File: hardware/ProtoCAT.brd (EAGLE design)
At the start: 59.7 x 53.3 mm, 47 parts, among them U1 ARDUINO, U3 TB6621FNG

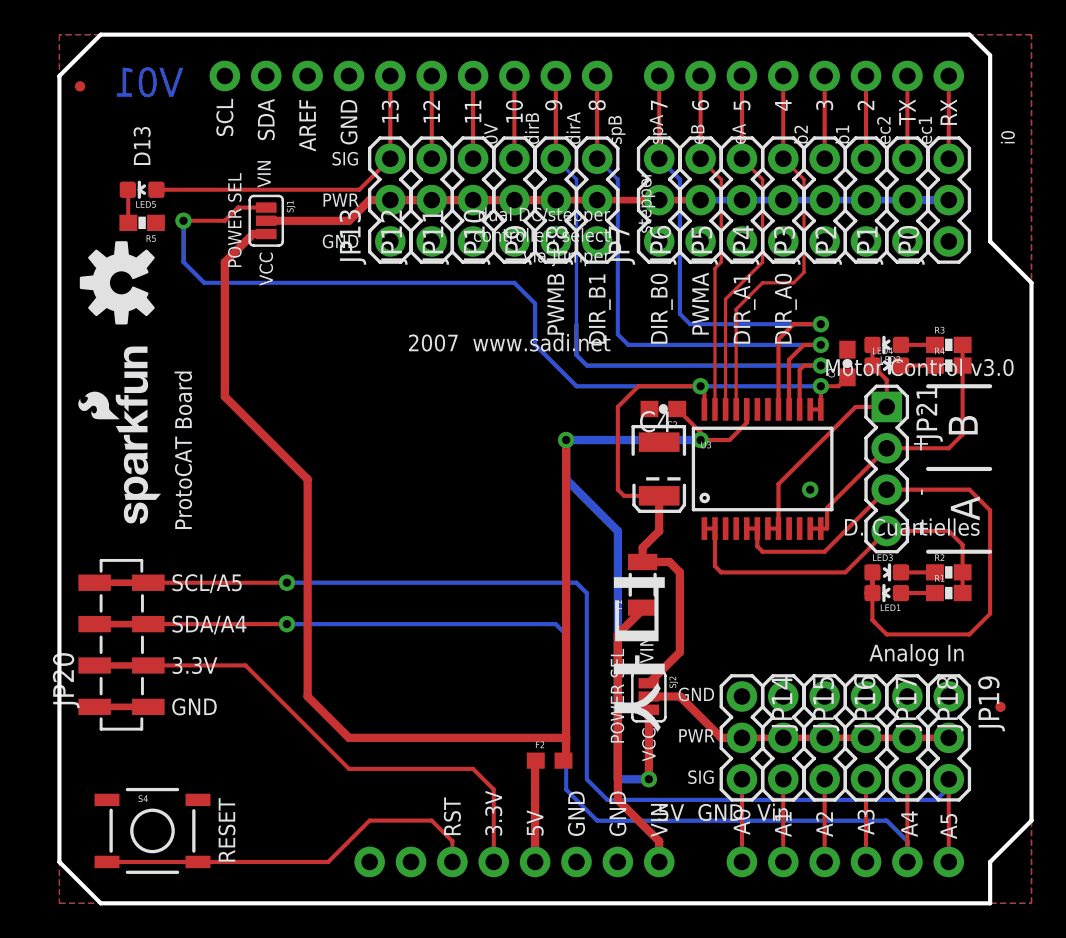
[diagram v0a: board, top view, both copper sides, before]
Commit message: Updates per - engineering review mtg 8/18
added prototyping area
added cut/solder jumpers for A4/A5 SDA/SCL lines for Leo
added ~PWM labels on pins 3, 5, 6, 9, 10, 11
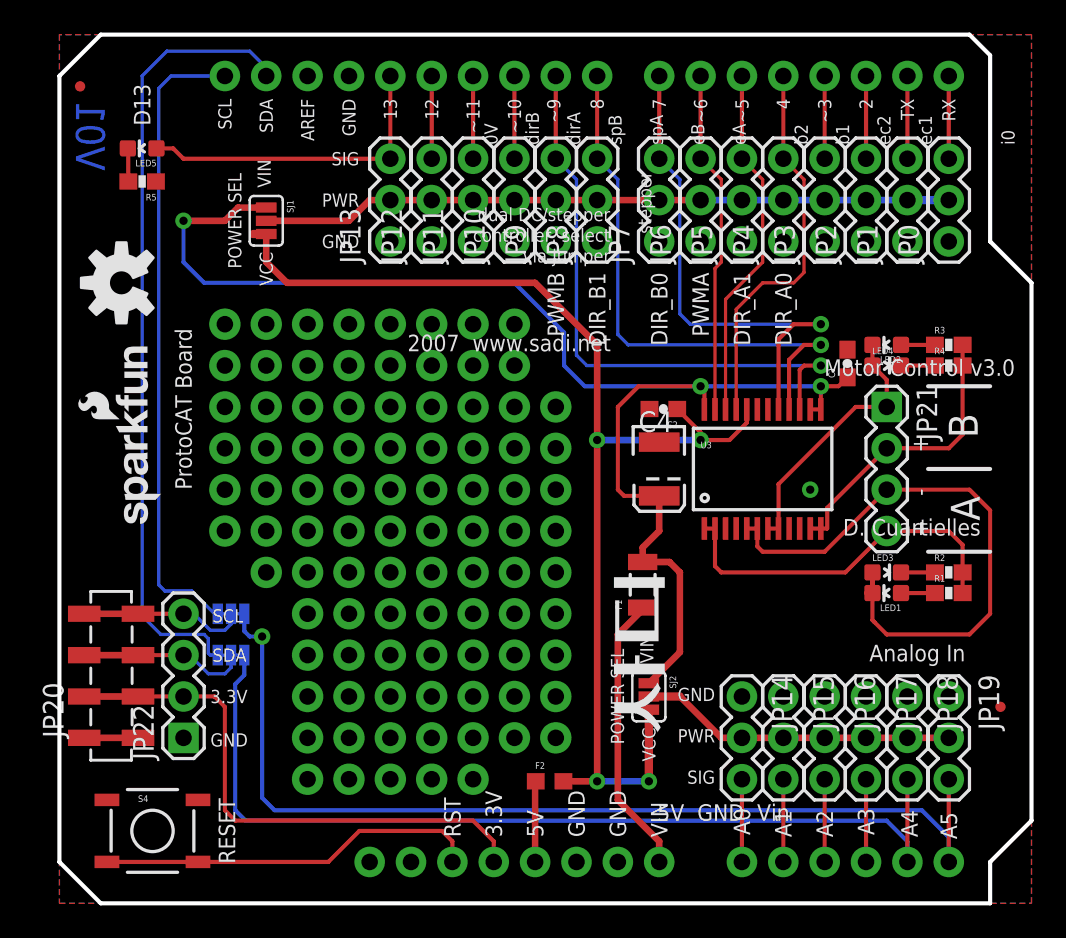
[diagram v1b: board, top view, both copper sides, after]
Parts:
- added JP22: (no value), SparkFun-Connectors:1X04
- added SJ3, SJ4: (no value), SparkFun-Passives:PAD-JUMPER-3-3OF3_NC_BY_TRACE_YES_SILK_FULL_BOX
- JP0: value (none) -> D0
- JP1: value (none) -> D1
- JP10: value (none) -> D10
- JP11: value (none) -> D11
- JP12: value (none) -> D12
- JP13: value (none) -> D13
- JP14: value (none) -> A0
- JP15: value (none) -> A1
- JP16: value (none) -> A2
- JP17: value (none) -> A3
- JP18: value (none) -> A4
- JP19: value (none) -> A5
- JP2: value (none) -> D2
- JP3: value (none) -> D3
- JP4: value (none) -> D4
- JP5: value (none) -> D5
- JP6: value (none) -> D6
- JP7: value (none) -> D7
- JP8: value (none) -> D8
- JP9: value (none) -> D9
- LED5: value (none) -> YELLOW
- LOGO2: value (none) -> SFE_LOGO_NAME_FLAME.1_INCH
- S4: value (none) -> RESET
- moved LED5 2.54 mm to (5.08, 46.4)
- moved R5 2.54 mm to (5.08, 44.3)
- moved JP20 2.01 mm to (3.17, 10.2)
- moved F2 1.27 mm to (30.1, 7.49)
- renumbered U$2 to LOGO2
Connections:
- new net SCL: SJ4.1, U1.SCL
- new net SCL_I2C_PORT: JP20.4, JP22.4, SJ4.2
- new net SDA: SJ3.1, U1.SDA
- new net SDA_I2C_PORT: JP20.3, JP22.3, SJ3.2
- net 3.3V: now also JP22.2
- net A4: now also SJ3.3; no longer JP20.3
- net A5: now also SJ4.3; no longer JP20.4
- net GND: now also JP22.1
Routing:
- net SDA: track 0.00 -> 48.5 mm
- net SCL: track 0.00 -> 39.2 mm
- net FUSED_VCC: track 112.2 -> 74.6 mm, vias 3 -> 4
- net SCL_I2C_PORT: track 0.00 -> 10.2 mm
- net A5: track 70.6 -> 62.0 mm
- net SDA_I2C_PORT: track 0.00 -> 7.11 mm
- net A4: track 64.1 -> 58.2 mm, vias 1 -> 0
- net 3.3V: track 32.1 -> 33.8 mm
- net VCC: track 6.26 -> 4.97 mm
- net D13: track 20.2 -> 19.7 mm
- net RESET: track 24.1 -> 23.5 mm
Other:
- board text added: "~10"
- board text added: "~11"
- board text added: "~3"
- board text added: "~5"
- board text added: "~6"
- board text added: "~9"
- board text removed: "10"
- board text removed: "11"
- board text removed: "3"
- board text removed: "5"
- board text removed: "6"
- board text removed: "9"
- board text removed: "SCL/A5"
- board text removed: "SDA/A4"

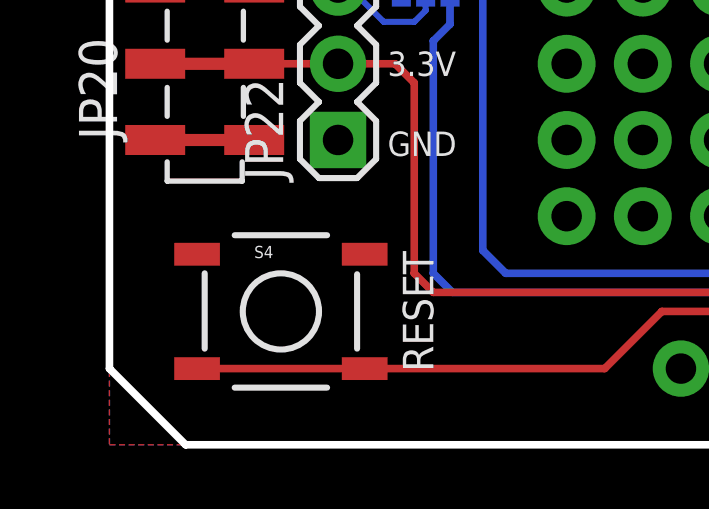
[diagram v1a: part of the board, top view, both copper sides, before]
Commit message: Updated a few aesthetic elements on bottom side
Included Ludus and sparkfun logo on bottom layer
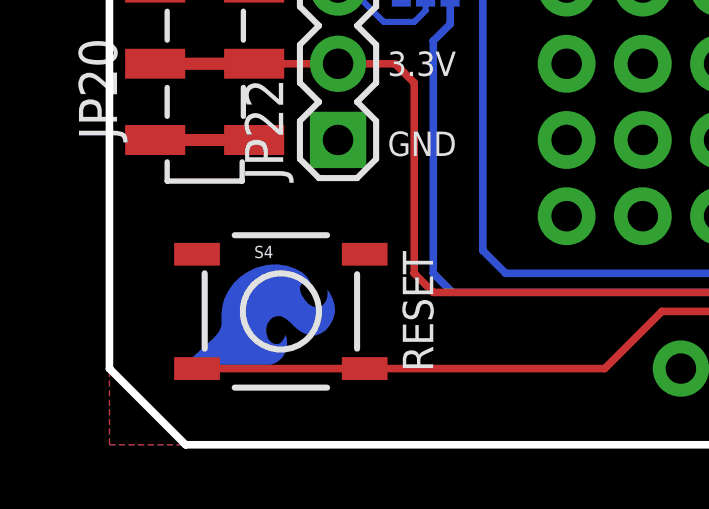
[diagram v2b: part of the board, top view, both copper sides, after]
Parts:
- added LOGO3: SFE_LOGO_FLAME.2COP, SparkFun-Aesthetics:SFE_LOGO_FLAME_COPPER_.2
- added LOGO4: SFE_LOGO_NAME_FLAME.1_INCH, SparkFun-Aesthetics:SFE_LOGO_NAME_FLAME_.1
- added U$1: SFE_LUDUS, SparkFun-Aesthetics:SFE_LUDUS-M
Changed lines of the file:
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@@
 <grid distance="0.05" unitdist="inch" unit="inch" style="dots" multiple="1" display="yes" altdistance="0.005" altunitdist="inch" altunit="inch"/>
 <layers>
-<layer number="1" name="Top" color="4" fill="1" visible="yes" active="yes"/>
+<layer number="1" name="Top" color="4" fill="1" visible="no" active="yes"/>
 <layer number="2" name="Route2" color="1" fill="3" visible="no" active="yes"/>
 <layer number="15" name="Route15" color="4" fill="6" visible="no" active="yes"/>
 <layer number="16" name="Bottom" color="1" fill="1" visible="yes" active="yes"/>
-<layer number="17" name="Pads" color="2" fill="1" visible="yes" active="yes"/>
+<layer number="17" name="Pads" color="2" fill="1" visible="no" active="yes"/>
 <layer number="18" name="Vias" color="2" fill="1" visible="yes" active="yes"/>
-<layer number="19" name="Unrouted" color="6" fill="1" visible="yes" active="yes"/>
+<layer number="19" name="Unrouted" color="6" fill="1" visible="no" active="yes"/>
 <layer number="20" name="Dimension" color="15" fill="1" visible="yes" active="yes"/>
-<layer number="21" name="tPlace" color="16" fill="1" visible="yes" active="yes"/>
+<layer number="21" name="tPlace" color="16" fill="1" visible="no" active="yes"/>
 <layer number="22" name="bPlace" color="14" fill="1" visible="yes" active="yes"/>
-<layer number="23" name="tOrigins" color="15" fill="1" visible="yes" active="yes"/>
+<layer number="23" name="tOrigins" color="15" fill="1" visible="no" active="yes"/>
 <layer number="24" name="bOrigins" color="15" fill="1" visible="yes" active="yes"/>
 <layer number="25" name="tNames" color="7" fill="1" visible="no" active="yes"/>
@@
 <layer number="43" name="vRestrict" color="2" fill="10" visible="no" active="yes"/>
 <layer number="44" name="Drills" color="7" fill="1" visible="no" active="yes"/>
-<layer number="45" name="Holes" color="7" fill="1" visible="yes" active="yes"/>
+<layer number="45" name="Holes" color="7" fill="1" visible="no" active="yes"/>
 <layer number="46" name="Milling" color="3" fill="1" visible="no" active="yes"/>
-<layer number="51" name="tDocu" color="6" fill="1" visible="yes" active="yes"/>
+<layer number="51" name="tDocu" color="6" fill="1" visible="no" active="yes"/>
 <layer number="52" name="bDocu" color="7" fill="1" visible="no" active="yes"/>
 <layer number="3" name="Route3" color="4" fill="3" visible="no" active="no"/>
@@
 <element name="SJ3" library="SparkFun-Passives" package="PAD-JUMPER-3-3OF3_NC_BY_TRACE_YES_SILK_FULL_BOX" value="" x="10.541" y="15.24" rot="MR180"/>
 <element name="SJ4" library="SparkFun-Passives" package="PAD-JUMPER-3-3OF3_NC_BY_TRACE_YES_SILK_FULL_BOX" value="" x="10.541" y="17.78" rot="MR180"/>
+<element name="U$1" library="SparkFun-Aesthetics" package="SFE_LUDUS-M" value="SFE_LUDUS" x="41.91" y="24.13" rot="MR90"/>
+<element name="LOGO3" library="SparkFun-Aesthetics" package="SFE_LOGO_FLAME_COPPER_.2" value="SFE_LOGO_FLAME.2COP" x="2.159" y="2.286" rot="SMR90"/>
+<element name="LOGO4" library="SparkFun-Aesthetics" package="SFE_LOGO_NAME_FLAME_.1" value="SFE_LOGO_NAME_FLAME.1_INCH" x="53.34" y="19.05" rot="MR90"/>
 </elements>
 <signals>

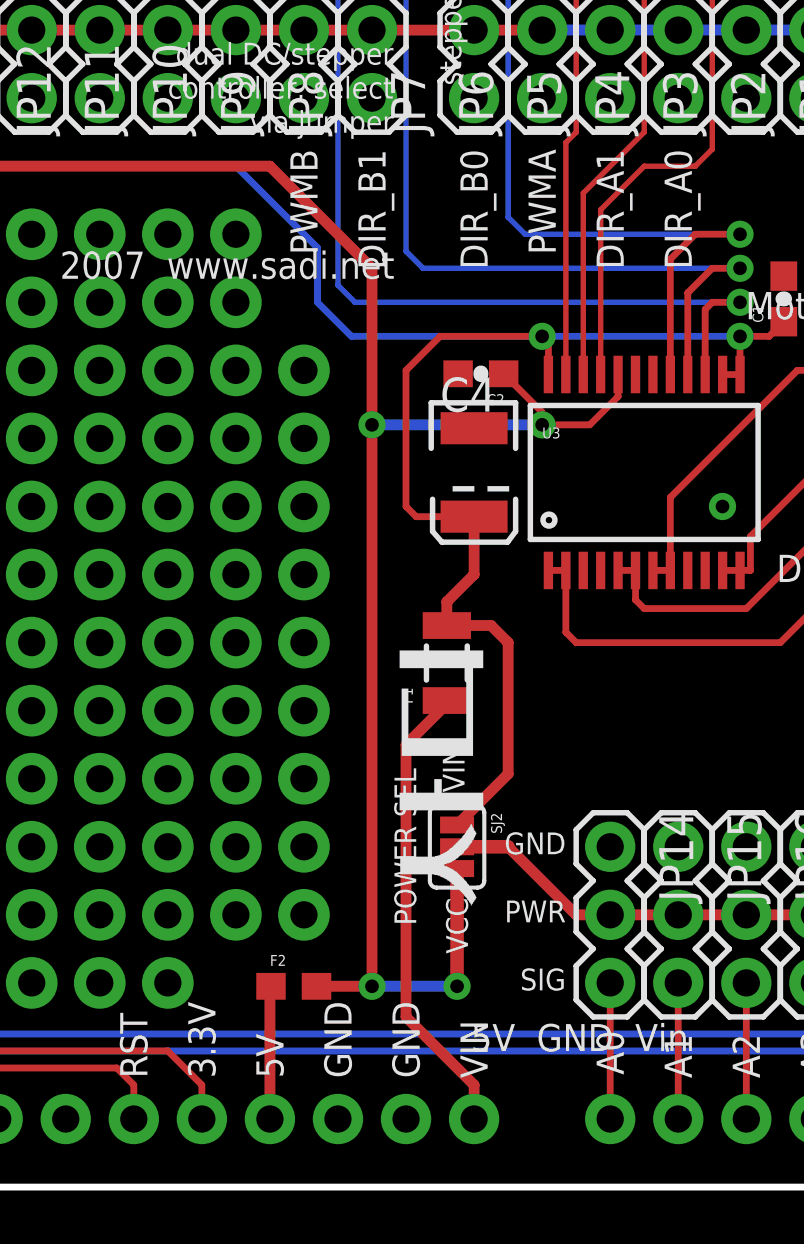
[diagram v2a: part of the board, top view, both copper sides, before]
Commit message: Updated fuse to 1206 part on Vcc Line
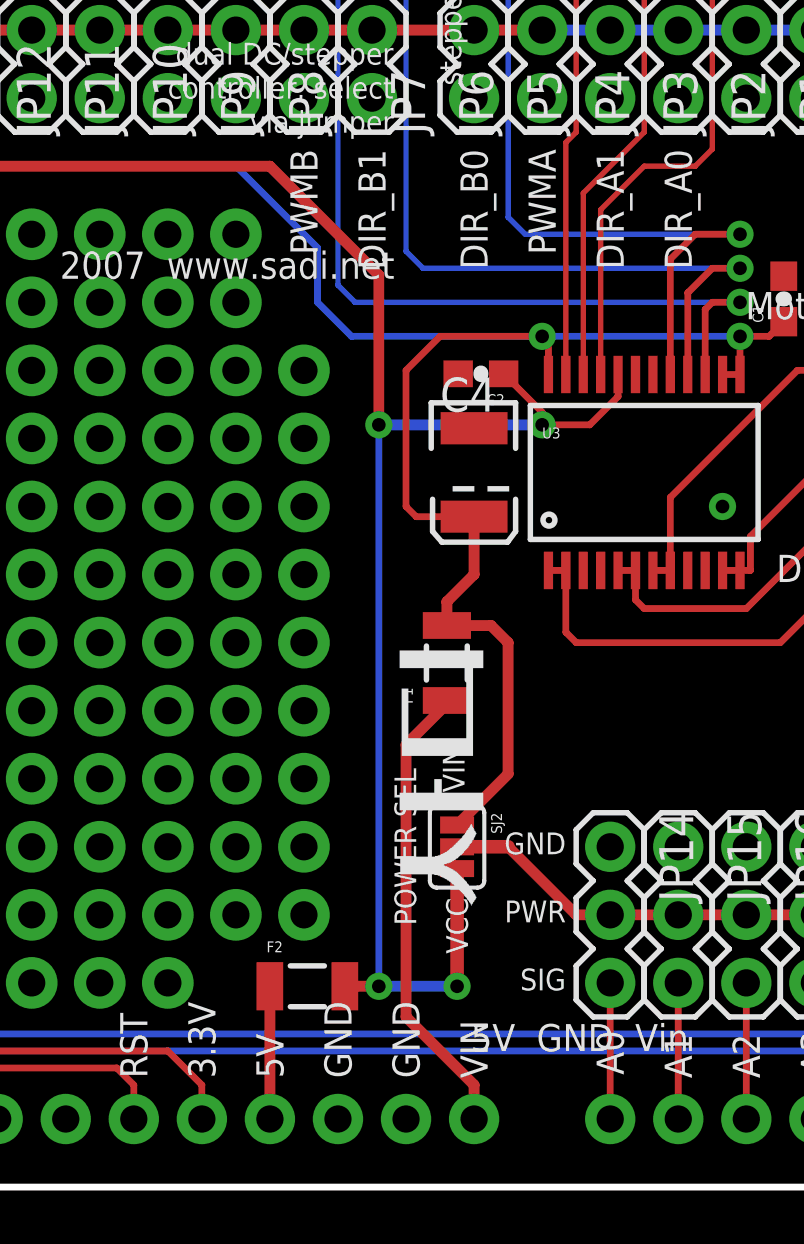
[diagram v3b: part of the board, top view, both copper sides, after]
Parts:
- F2: value PTC0603 -> PTCSMD; device SparkFun-PowerIC:0603 -> SparkFun-PowerIC:PTC-1206
- LED5: value YELLOW -> Blue
- U3: value TB6621FNG -> (none); device SparkFun:SSOP24 -> SparkFun-PowerIC:SSOP24
- moved F2 0.51 mm to (30.6, 7.49)
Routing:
- net FUSED_VCC: track 74.6 -> 73.4 mm
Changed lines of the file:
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@@
 <grid distance="0.05" unitdist="inch" unit="inch" style="dots" multiple="1" display="yes" altdistance="0.005" altunitdist="inch" altunit="inch"/>
 <layers>
-<layer number="1" name="Top" color="4" fill="1" visible="no" active="yes"/>
+<layer number="1" name="Top" color="4" fill="1" visible="yes" active="yes"/>
 <layer number="2" name="Route2" color="1" fill="3" visible="no" active="yes"/>
 <layer number="15" name="Route15" color="4" fill="6" visible="no" active="yes"/>
 <layer number="16" name="Bottom" color="1" fill="1" visible="yes" active="yes"/>
-<layer number="17" name="Pads" color="2" fill="1" visible="no" active="yes"/>
+<layer number="17" name="Pads" color="2" fill="1" visible="yes" active="yes"/>
 <layer number="18" name="Vias" color="2" fill="1" visible="yes" active="yes"/>
-<layer number="19" name="Unrouted" color="6" fill="1" visible="no" active="yes"/>
+<layer number="19" name="Unrouted" color="6" fill="1" visible="yes" active="yes"/>
 <layer number="20" name="Dimension" color="15" fill="1" visible="yes" active="yes"/>
-<layer number="21" name="tPlace" color="16" fill="1" visible="no" active="yes"/>
+<layer number="21" name="tPlace" color="16" fill="1" visible="yes" active="yes"/>
 <layer number="22" name="bPlace" color="14" fill="1" visible="yes" active="yes"/>
-<layer number="23" name="tOrigins" color="15" fill="1" visible="no" active="yes"/>
+<layer number="23" name="tOrigins" color="15" fill="1" visible="yes" active="yes"/>
 <layer number="24" name="bOrigins" color="15" fill="1" visible="yes" active="yes"/>
 <layer number="25" name="tNames" color="7" fill="1" visible="no" active="yes"/>
@@
 <layer number="43" name="vRestrict" color="2" fill="10" visible="no" active="yes"/>
 <layer number="44" name="Drills" color="7" fill="1" visible="no" active="yes"/>
-<layer number="45" name="Holes" color="7" fill="1" visible="no" active="yes"/>
+<layer number="45" name="Holes" color="7" fill="1" visible="yes" active="yes"/>
 <layer number="46" name="Milling" color="3" fill="1" visible="no" active="yes"/>
-<layer number="51" name="tDocu" color="6" fill="1" visible="no" active="yes"/>
+<layer number="51" name="tDocu" color="6" fill="1" visible="yes" active="yes"/>
 <layer number="52" name="bDocu" color="7" fill="1" visible="no" active="yes"/>
 <layer number="3" name="Route3" color="4" fill="3" visible="no" active="no"/>
@@
 <element name="JP4" library="SparkFun-Connectors" package="1X03" value="D4" x="44.45" y="40.64" rot="R90"/>
 <element name="JP5" library="SparkFun-Connectors" package="1X03" value="D5" x="41.91" y="40.64" rot="R90"/>
-<element name="U3" library="SparkFun" package="SSOP24" value="TB6621FNG" x="43.18" y="26.67"/>
+<element name="U3" library="SparkFun-PowerIC" package="SSOP24" value="" x="43.18" y="26.67">
+<attribute name="PROD_ID" value="IC-09363" x="43.18" y="26.67" size="1.778" layer="27" display="off"/>
+<attribute name="VALUE" value="TB6612FNG" x="43.18" y="26.67" size="1.778" layer="27" display="off"/>
+</element>
 <element name="C1" library="SparkFun-Capacitors" package="0603-CAP" value="0.1uF" x="48.387" y="33.147" rot="R90">
 <attribute name="PROD_ID" value="CAP-08604" x="48.387" y="33.147" size="1.778" layer="27" rot="R90" display="off"/>
@@
 <element name="JP18" library="SparkFun-Connectors" package="1X03" value="A4" x="52.07" y="12.7" rot="R270"/>
 <element name="JP19" library="SparkFun-Connectors" package="1X03" value="A5" x="54.61" y="12.7" rot="R270"/>
-<element name="LED5" library="SparkFun-LED" package="LED-0603" value="YELLOW" x="5.08" y="46.355" rot="R90"/>
+<element name="LED5" library="SparkFun-LED" package="LED-0603" value="Blue" x="5.08" y="46.355" rot="R90"/>
 <element name="R5" library="SparkFun-Resistors" package="0603-RES" value="330" x="5.08" y="44.323" rot="R180">
 <attribute name="PROD_ID" value="RES-00818" x="5.08" y="44.323" size="1.778" layer="27" rot="R180" display="off"/>
@@
 <attribute name="PROD_ID" value="RES-11150" x="35.814" y="19.558" size="1.778" layer="27" rot="R90" display="off"/>
 </element>
-<element name="F2" library="SparkFun-PowerIC" package="0603" value="PTC0603" x="30.099" y="7.493"/>
+<element name="F2" library="SparkFun-PowerIC" package="PTC-1206" value="PTCSMD" x="30.607" y="7.493">
+<attribute name="PROD_ID" value="RES-11150" x="30.607" y="7.493" size="1.778" layer="27" display="off"/>
+</element>
 <element name="FID1" library="SparkFun-Aesthetics" package="MICRO-FIDUCIAL" value="FIDUCIALUFIDUCIAL" x="1.27" y="50.165"/>
 <element name="FID2" library="SparkFun-Aesthetics" package="MICRO-FIDUCIAL" value="FIDUCIALUFIDUCIAL" x="57.785" y="12.065"/>
@@
 <contactref element="U1" pad="5V"/>
 <contactref element="F2" pad="1"/>
-<wire x1="29.21" y1="2.54" x2="29.21" y2="7.454" width="0.4064" layer="1"/>
-<wire x1="29.21" y1="7.454" x2="29.249" y2="7.493" width="0.4064" layer="1"/>
+<wire x1="29.207" y1="7.493" x2="29.207" y2="2.543" width="0.4064" layer="1"/>
+<wire x1="29.207" y1="2.543" x2="29.21" y2="2.54" width="0.4064" layer="1"/>
 </signal>
 <signal name="D10">
@@
 <contactref element="SJ2" pad="3"/>
 <wire x1="12.7" y1="41.0972" x2="11.8872" y2="41.0972" width="0.508" layer="1"/>
-<via x="33.02" y="28.448" extent="1-16" drill="0.508"/>
-<wire x1="33.02" y1="28.448" x2="39.37" y2="28.448" width="0.4064" layer="16"/>
+<via x="33.274" y="28.448" extent="1-16" drill="0.508"/>
+<wire x1="33.274" y1="28.448" x2="39.37" y2="28.448" width="0.4064" layer="16"/>
 <wire x1="39.37" y1="28.448" x2="41.148" y2="28.448" width="0.254" layer="1"/>
 <wire x1="41.148" y1="28.448" x2="42.205" y2="29.505" width="0.254" layer="1"/>
@@
 <wire x1="36.195" y1="11.8872" x2="36.195" y2="7.493" width="0.508" layer="1"/>
 <via x="36.195" y="7.493" extent="1-16" drill="0.508"/>
-<wire x1="33.02" y1="34.29" x2="29.21" y2="38.1" width="0.4064" layer="1"/>
+<wire x1="33.274" y1="34.036" x2="29.21" y2="38.1" width="0.4064" layer="1"/>
 <wire x1="29.21" y1="38.1" x2="13.97" y2="38.1" width="0.4064" layer="1"/>
 <wire x1="12.7" y1="41.0972" x2="12.7" y2="39.37" width="0.4064" layer="1"/>
 <wire x1="12.7" y1="39.37" x2="13.97" y2="38.1" width="0.4064" layer="1"/>
-<wire x1="33.02" y1="28.448" x2="33.02" y2="34.29" width="0.4064" layer="1"/>
-<via x="33.02" y="7.493" extent="1-16" drill="0.508" diameter="1.016"/>
-<wire x1="30.949" y1="7.493" x2="33.02" y2="7.493" width="0.4064" layer="1"/>
-<wire x1="33.02" y1="7.493" x2="36.195" y2="7.493" width="0.4064" layer="16"/>
-<wire x1="33.02" y1="7.493" x2="33.02" y2="28.448" width="0.4064" layer="1"/>
+<via x="33.274" y="7.493" extent="1-16" drill="0.508" diameter="1.016"/>
+<wire x1="32.007" y1="7.493" x2="33.274" y2="7.493" width="0.4064" layer="1"/>
+<wire x1="33.274" y1="7.493" x2="36.195" y2="7.493" width="0.4064" layer="16"/>
+<wire x1="33.274" y1="28.448" x2="33.274" y2="7.493" width="0.254" layer="16"/>
+<wire x1="33.274" y1="28.448" x2="33.274" y2="34.036" width="0.4064" layer="1"/>
 </signal>
 <signal name="PWR_RAIL">
